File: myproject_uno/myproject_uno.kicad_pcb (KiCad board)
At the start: 2 copper layers, 68.6 x 53.3 mm, 10 parts, among them P1 Power, P2 Analog, P3 Digital, P4 Digital, P5 CONN_01X01, P6 CONN_01X01, P7 CONN_01X01, P8 CONN_01X01

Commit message: pcb almost designed
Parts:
- removed D1: LED, LED_SMD:LED_0201_0603Metric
- added C1: 100n, Capacitor_SMD:C_0603_1608Metric, F.Cu at (160.6, 105.2)
- added C2: 100n, Capacitor_SMD:C_0603_1608Metric, F.Cu at (164.9, 95.8)
- added C3: 100n, Capacitor_SMD:C_0603_1608Metric, F.Cu at (173.5, 95.8)
- added C4: 1u, Capacitor_SMD:C_0603_1608Metric, F.Cu at (169.8, 111.6)
- added C8: 0,1u, Capacitor_SMD:C_0603_1608Metric, F.Cu at (160.3, 84.9)
- added J1: Conn_Coaxial, Connector_Coaxial:SMA_Amphenol_132289_EdgeMount, F.Cu at (114.1, 101.9)
- added R3: 100K, Resistor_SMD:R_0603_1608Metric, F.Cu at (173.0, 111.6)
- added R5: 100K, Resistor_SMD:R_0603_1608Metric, F.Cu at (160.6, 110.3)
- added R6: 1K, Resistor_SMD:R_0603_1608Metric, F.Cu at (166.5, 111.6)
- added R7: 10K, Resistor_SMD:R_0603_1608Metric, F.Cu at (137.3, 102.2)
- added R8: 100K, Resistor_SMD:R_0603_1608Metric, F.Cu at (160.3, 82.6)
- added Rcal1: R, Resistor_SMD:R_0603_1608Metric, F.Cu at (167.9, 95.8)
- added Rcal2: R, Resistor_SMD:R_0603_1608Metric, F.Cu at (170.8, 95.8)
- added Rsensor1: R, Package_TO_SOT_THT:TO-5-4, F.Cu at (145.2, 108.2)
- added U1: LTC1050, Package_DIP:DIP-8_W7.62mm_LongPads, F.Cu at (165.4, 100.3)
- added U2: RN2483, RF_Module:RN2483, F.Cu at (142.5, 90.8)
- added U3: LTC1050, Package_DIP:DIP-8_W7.62mm_LongPads, F.Cu at (164.0, 82.3)
- R1: value R -> 100K; footprint Resistor_SMD:R_0201_0603Metric -> Resistor_SMD:R_0603_1608Metric
- moved R1 6.14 mm to (160.6, 107.7)
- moved P1 1.89 mm to (139.2, 125.7)
- moved P4 1.89 mm to (157.0, 77.4)
- moved P2 1.89 mm to (162.1, 125.7)
- moved P3 1.89 mm to (130.1, 77.4)
- moved P5 1.89 mm to (125.2, 125.7)
- moved P6 1.89 mm to (177.3, 120.6)
- moved P7 1.89 mm to (126.5, 77.4)
- moved P8 1.89 mm to (177.3, 92.7)
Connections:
- P2 pad 1: /A0 -> ANxArduino
- P3 pad 6: /12(MISO) -> !RST
- P3 pad 7: /11(**/MOSI) -> RX
- P3 pad 8: /10(**/SS) -> TX
- P4 pad 2: /6(**) -> Vref
- P4 pad 6: /2 -> INT
- R1 pad 1: /Vin -> Net-(C1-Pad1)
- R1 pad 2: Net-(D1-Pad2) -> GND
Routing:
- net +5V: track 0.00 -> 87.1 mm
- net ANxArduino: track 0.00 -> 61.3 mm
- net +3V3: track 0.00 -> 57.7 mm
- net !RST: track 0.00 -> 44.6 mm
- net Net-(J1-Pad1): track 0.00 -> 22.4 mm
- net Net-(C4-Pad1): track 0.00 -> 21.3 mm
- net Net-(C4-Pad2): track 0.00 -> 16.1 mm
- net /Vin: track 14.2 -> 0.15 mm
- net INT: track 0.00 -> 14.0 mm
- net GND: track 13.9 -> 0.00 mm, vias 0 -> 8
- net Net-(R5-Pad1): track 0.00 -> 12.3 mm
- net Net-(C1-Pad1): track 0.00 -> 9.97 mm
- net Net-(C8-Pad1): track 0.00 -> 5.21 mm
- net Vref: track 0.00 -> 5.17 mm
- net RX: track 0.00 -> 4.61 mm
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- added copper zone on F.Cu, net GND
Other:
- board size 68.6 x 53.3 mm -> 68.6 x 63.4 mm

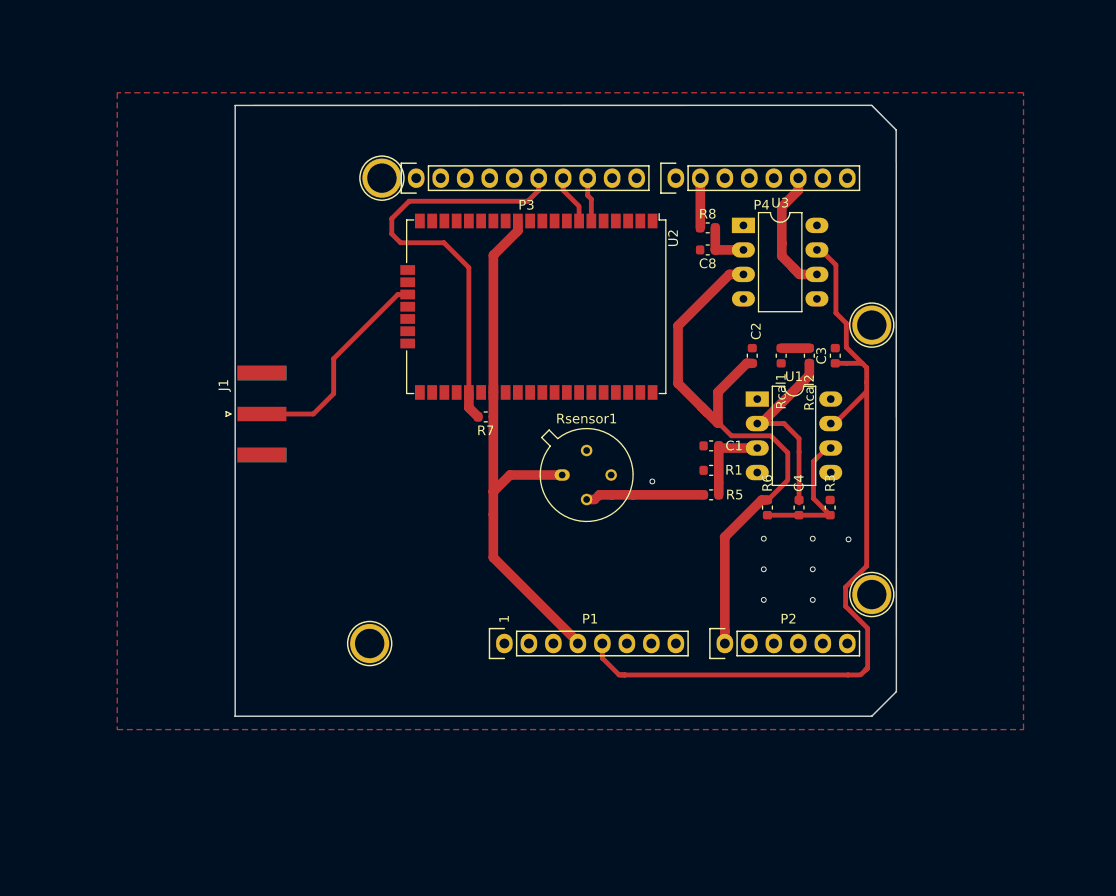
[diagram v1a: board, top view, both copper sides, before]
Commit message: pcb redesigned and resized, gnd plane missing
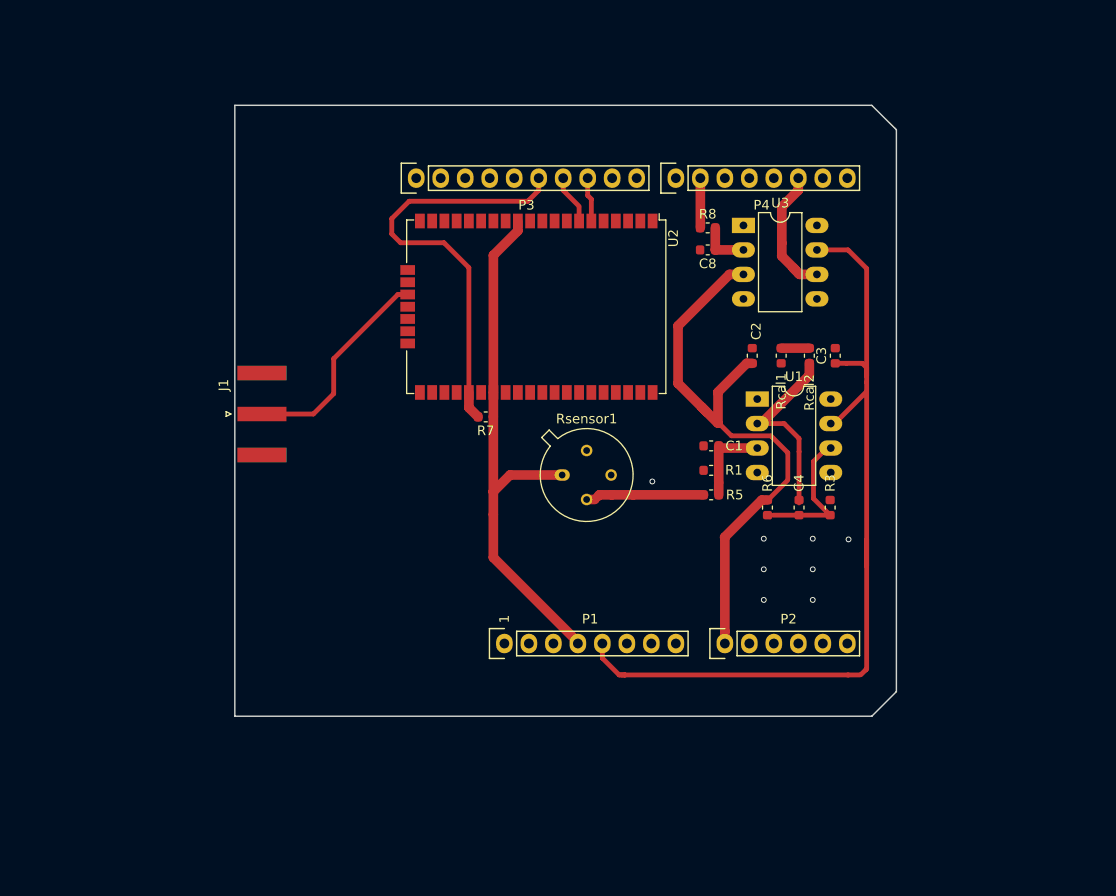
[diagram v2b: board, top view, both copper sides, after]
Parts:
- removed P5, P6, P7, P8: CONN_01X01, Socket_Arduino_Uno:Arduino_1pin
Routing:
- net +5V: track 87.1 -> 91.2 mm
- removed copper zone on F.Cu, net GND
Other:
- outline, holes or cut-outs redrawn

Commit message: last version of PCB
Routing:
- net ANxArduino: track 61.3 -> 79.0 mm
- net !RST: track 44.6 -> 52.3 mm
- net Net-(R5-Pad1): track 12.3 -> 17.6 mm
- net +5V: track 91.2 -> 92.4 mm
- net GND: vias 8 -> 1
- added copper zone on F.Cu, net GND

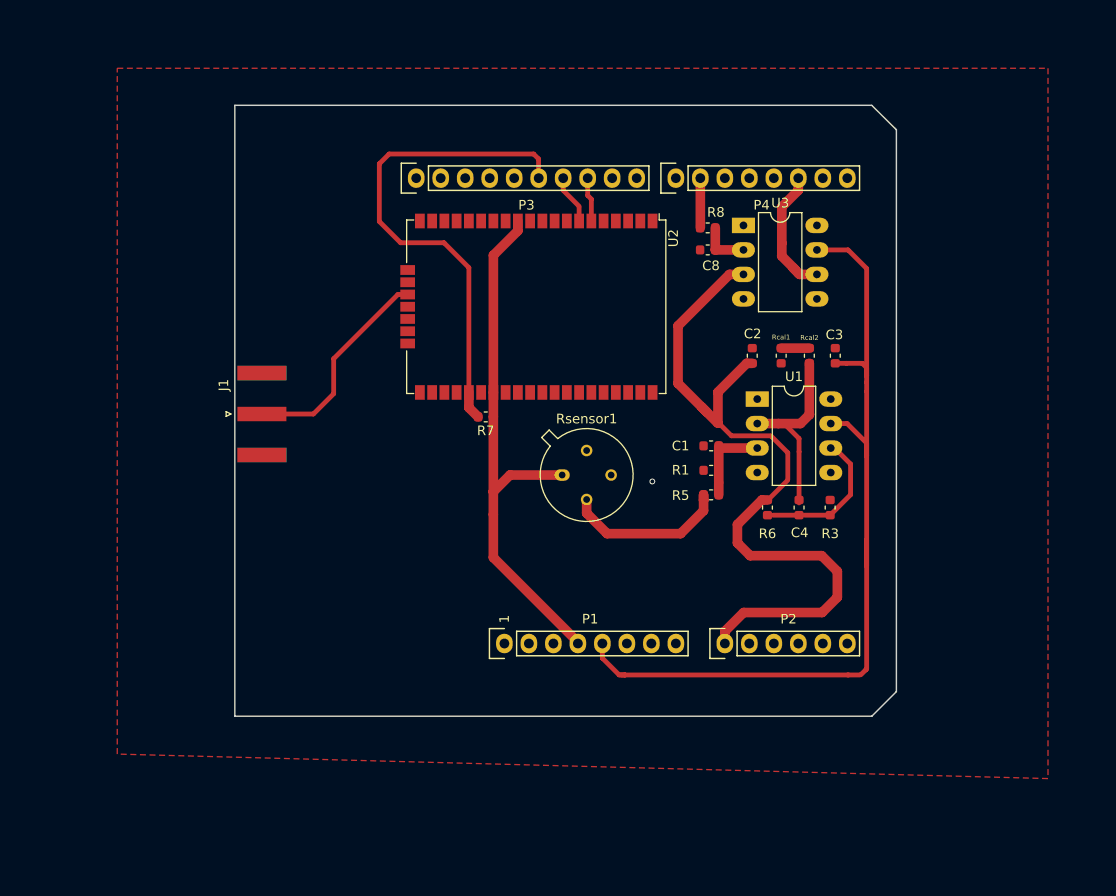
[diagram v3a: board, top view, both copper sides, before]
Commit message: pcb with 8 pins
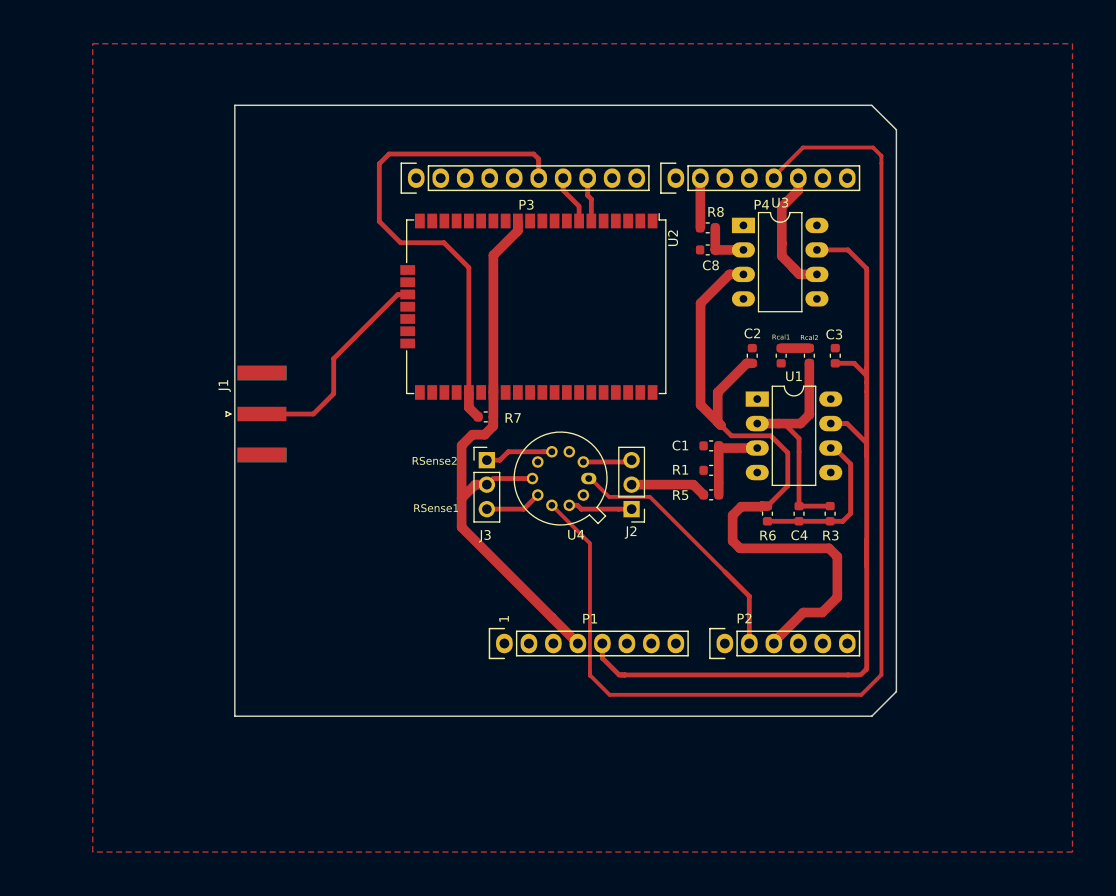
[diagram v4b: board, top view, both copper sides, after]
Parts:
- removed Rsensor1: R, Package_TO_SOT_THT:TO-5-4
- added J2: Conn_01x03, Connector_PinHeader_2.54mm:PinHeader_1x03_P2.54mm_Vertical, F.Cu at (152.4, 111.8)
- added J3: Conn_01x03, Connector_PinHeader_2.54mm:PinHeader_1x03_P2.54mm_Vertical, F.Cu at (137.4, 106.7)
- added U4: GazSensor, Package_TO_SOT_THT:TO-5-10, F.Cu at (148.0, 108.6)
- U2: footprint RF_Module:RN2483 -> RN2483
- moved C4 0.63 mm to (169.8, 112.2)
- moved R3 0.63 mm to (173.0, 112.2)
- moved R6 0.63 mm to (166.5, 112.2)
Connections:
- P1 pad 5: +5V -> Net-(P1-Pad5)
- P2 pad 1: ANxArduino -> /A0
- P2 pad 2: /A1 -> CapTemp
- P2 pad 3: /A2 -> ANxArduino
- P4 pad 5: /3(**) -> RChauff
- R3 pad 1: Net-(R3-Pad1) -> Net-(C4-Pad1)
- R5 pad 1: Net-(R5-Pad1) -> Rsensor
- U1 pad 5: Net-(U1-Pad5) -> GND
- U2 pad 11: GND -> Net-(U2-Pad11)
- U2 pad 20: GND -> Net-(U2-Pad20)
- U2 pad 21: GND -> Net-(U2-Pad21)
- U2 pad 22: GND -> Net-(U2-Pad22)
- U2 pad 41: GND -> Net-(U2-Pad41)
- U3 pad 5: Net-(U3-Pad5) -> GND
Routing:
- net RChauff: track 0.00 -> 118.2 mm
- net CapTemp: track 0.00 -> 26.8 mm
- net Net-(R5-Pad1): track 17.6 -> 0.00 mm
- net Rsensor: track 0.00 -> 7.90 mm
- net Net-(J3-Pad1): track 0.00 -> 7.11 mm
- net Net-(J2-Pad1): track 0.00 -> 6.63 mm
- net Net-(J3-Pad3): track 0.00 -> 5.89 mm
- net ANxArduino: track 79.0 -> 73.6 mm
- net Net-(J2-Pad3): track 0.00 -> 5.08 mm
- net Net-(C4-Pad1): track 21.3 -> 24.9 mm
- net +3V3: track 57.7 -> 60.4 mm
- net Net-(C4-Pad2): track 16.3 -> 17.7 mm
- net /A0: track 0.00 -> 0.71 mm
- net GND: vias 1 -> 0
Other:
- board text added: "RSense1"
- board text added: "RSense2"

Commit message: final version
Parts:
- removed J1: Conn_Coaxial, Connector_Coaxial:SMA_Amphenol_132289_EdgeMount
- added Antenna: Conn_Coaxial, Connector_Coaxial:SMA_Molex_73251-1153_EdgeMount_Horizontal, F.Cu at (116.0, 89.5)
- C1, C2, C3, C4, C8: footprint Capacitor_SMD:C_0603_1608Metric -> Capacitor_SMD:C_1206_3216Metric
- Gas Sensor: renamed from U4
- R1, R3, R5, R6, R7, R8, Rcal1, Rcal2: footprint Resistor_SMD:R_0603_1608Metric -> Resistor_SMD:R_1206_3216Metric
- moved J2 1.45 mm to (153.8, 111.6)
- moved C1 1.06 mm to (160.0, 104.3)
- moved C3 0.96 mm to (174.5, 95.8)
- moved R5 0.76 mm to (160.1, 110.8)
- moved R1 0.70 mm to (160.1, 107.3)
- moved R8 0.56 mm to (160.0, 82.1)
- moved C2 0.52 mm to (165.4, 95.9)
- moved Rcal1 0.40 mm to (168.3, 95.9)
- moved U3 0.33 mm to (164.3, 82.2)
- moved C8 0.26 mm to (160.1, 85.0)
- moved Rcal2 0.26 mm to (171.1, 95.8)
- moved R7 0.20 mm to (137.1, 102.3)
- moved U1 0.12 mm to (165.5, 100.4)
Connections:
- U2 pad 23: Net-(J1-Pad1) -> ANT
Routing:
- net ANxArduino: track 73.6 -> 48.1 mm, vias 0 -> 2
- net Net-(J1-Pad1): track 22.4 -> 0.00 mm
- net +3V3: track 60.4 -> 78.8 mm
- net ANT: track 0.00 -> 15.9 mm
- net CapTemp: track 26.8 -> 30.6 mm, vias 0 -> 2
- net !RST: track 52.3 -> 55.7 mm
- net RChauff: track 118.2 -> 120.9 mm, vias 0 -> 2
- net Net-(J2-Pad1): track 6.63 -> 8.95 mm
- net Rsensor: track 7.90 -> 5.63 mm
- net Net-(C4-Pad1): track 24.9 -> 23.2 mm
- net Net-(J2-Pad3): track 5.08 -> 6.60 mm
- net Net-(C1-Pad1): track 9.97 -> 11.1 mm
- net +5V: track 92.7 -> 91.7 mm
- net Net-(C8-Pad1): track 5.21 -> 5.81 mm
- net RX: track 4.61 -> 5.13 mm
- added copper zone on B.Cu, net GND
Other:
- board text added: "DUPOUY Sylvain GUILLARD Flavien Gas Sensor Board"
